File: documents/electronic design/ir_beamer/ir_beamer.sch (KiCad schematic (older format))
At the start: 42 parts, among them P1 Via, P10 Via, P2 Via, P3 Via, P4 Via, P5 Via, P7 Via, P8 Via, P9 Via, T1 2N7002K, T10 2N7002K, T11 2N7002K, T12 2N7002K, T2 2N7002K, T3 2N7002K, T4 2N7002K, T5 2N7002K, T6 2N7002K, T7 2N7002K, T8 2N7002K, T9 2N7002K, U1 74HC595D, U2 STM32F103HEADER, U3 74HC595D, U4 SE8R01_module

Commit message: update PCB projects for beamer and sensor
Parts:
- removed R1, R2, R3, R4: 4.7k, Resistors_SMD:R_0805_HandSoldering, symbol R
- added P11, P12, P13, P14, P15, P16, P17, P6: Via, footprints:Via, symbol Via
- R5: footprint (none) -> Resistors_SMD:R_0805_HandSoldering
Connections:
- net labels added: Cascade, MR_NOT, OE_NOT
- wire segments 10 -> 12
- no-connect marks 32 -> 30
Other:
- moved on the sheet: R5

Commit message: minor update in beamer pcb (added vias for pwm_gnd signal)
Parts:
- added P18, P19, P20, P21, P22, P23, P24, P25, P26, P27, P28: Via, footprints:Via, symbol Via
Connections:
- wire segments 12 -> 13

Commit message: update schema for receiver
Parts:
- removed P11, P12, P13, P15, P18, P19, P20, P21, P22, P23, P24, P25, P26, P27, P28, P6: Via, footprints:Via, symbol Via
- removed R5: 100, Resistors_SMD:R_0805_HandSoldering, symbol R
- removed T1, T10, T11, T12, T2, T3, T4, T5, T6, T7, T8, T9: 2N7002K, footprints:SOT23, symbol 2N7002K
- added R? (x4): 10K, symbol R
- added R? (x11): 50, symbol R
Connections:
- net labels removed: MR_NOT, OE_NOT, PWM_GND
- wire segments 13 -> 12
- no-connect marks 30 -> 32

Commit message: remake pcb for beamer
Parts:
- removed R? (x10): 50, symbol R
- added C2, C3: 100uf, Capacitors_SMD:C_1206_HandSoldering, symbol C
- added P11, P12, P13, P15, P18, P19, P20, P21, P6: Via, footprints:Via, symbol Via
- R1, R2, R3, R4, R5: renamed from R?; footprint (none) -> Capacitors_SMD:C_0805_HandSoldering
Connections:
- net labels added: IR_VCC
- wire segments 12 -> 36
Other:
- moved on the sheet: C1, D1, D10, D11, D2, D3, D4, D5, D6, D7, D8, D9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

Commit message: update pcb for beamer
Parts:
- removed P1, P10, P11, P12, P13, P14, P15, P16, P17, P18, P19, P2, P20, P21, P3, P4, P5, P6, P7, P8, P9: Via, footprints:Via, symbol Via
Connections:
- wire segments 36 -> 10

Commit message: fix beamer pcb
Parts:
- R1: value 50 -> 22
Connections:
- net labels added: IR_GND
- net labels removed: IR_VCC
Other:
- moved on the sheet: R1
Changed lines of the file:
@@
 F 3 "" H 1400 1150 50  0000 C CNN
 	1    1400 1150
-	-1   0    0    1
+	1    0    0    -1
 $EndComp
 Text Notes 8800 1650 0    60   ~ 0
@@
 F 3 "" H 1400 1750 50  0000 C CNN
 	1    1400 1750
-	-1   0    0    1
+	1    0    0    -1
 $EndComp
 Text GLabel 1600 1750 2    60   Input ~ 0
@@
 F 3 "" H 1400 2350 50  0000 C CNN
 	1    1400 2350
-	-1   0    0    1
+	1    0    0    -1
 $EndComp
 Text GLabel 1600 2350 2    60   Input ~ 0
@@
 F 3 "" H 1400 2950 50  0000 C CNN
 	1    1400 2950
-	-1   0    0    1
+	1    0    0    -1
 $EndComp
 Text GLabel 1600 2950 2    60   Input ~ 0
@@
 F 3 "" H 1400 3550 50  0000 C CNN
 	1    1400 3550
-	-1   0    0    1
+	1    0    0    -1
 $EndComp
 Text GLabel 1600 3550 2    60   Input ~ 0
@@
 F 3 "" H 1400 4150 50  0000 C CNN
 	1    1400 4150
-	-1   0    0    1
+	1    0    0    -1
 $EndComp
 Text GLabel 1600 4150 2    60   Input ~ 0
@@
 F 3 "" H 1400 4750 50  0000 C CNN
 	1    1400 4750
-	-1   0    0    1
+	1    0    0    -1
 $EndComp
 Text GLabel 1600 4750 2    60   Input ~ 0
@@
 F 3 "" H 1400 5350 50  0000 C CNN
 	1    1400 5350
-	-1   0    0    1
+	1    0    0    -1
 $EndComp
 Text GLabel 1600 5350 2    60   Input ~ 0
@@
 F 3 "" H 1400 5950 50  0000 C CNN
 	1    1400 5950
-	-1   0    0    1
+	1    0    0    -1
 $EndComp
 Text GLabel 1600 5950 2    60   Input ~ 0
@@
 F 3 "" H 1400 6550 50  0000 C CNN
 	1    1400 6550
-	-1   0    0    1
+	1    0    0    -1
 $EndComp
 Text GLabel 1600 6550 2    60   Input ~ 0
@@
 F 3 "" H 1400 7150 50  0000 C CNN
 	1    1400 7150
-	-1   0    0    1
+	1    0    0    -1
 $EndComp
 Text GLabel 4700 2700 2    60   Input ~ 0
@@
 	1    0    0    -1
 $EndComp
-$Comp
-L +5V #PWR012
-U 1 1 5791C22D
-P 1000 700
-F 0 "#PWR012" H 1000 550 50  0001 C CNN
-F 1 "+5V" H 1000 840 50  0000 C CNN
-F 2 "" H 1000 700 50  0000 C CNN
-F 3 "" H 1000 700 50  0000 C CNN
-	1    1000 700
-	0    -1   -1   0
-$EndComp
 Text GLabel 4700 1350 2    60   Input ~ 0
 Cascade
@@
 L R R1
 U 1 1 57A138ED
-P 1150 700
-F 0 "R1" V 1230 700 50  0000 C CNN
-F 1 "50" V 1150 700 50  0000 C CNN
-F 2 "Capacitors_SMD:C_0805_HandSoldering" V 1080 700 50  0001 C CNN
-F 3 "" H 1150 700 50  0000 C CNN
-	1    1150 700
-	0    1    1    0
-$EndComp
-Text GLabel 1300 700  2    60   Input ~ 0
-IR_VCC
-Text GLabel 1200 1150 0    60   Input ~ 0
-IR_VCC
-Text GLabel 1200 1750 0    60   Input ~ 0
-IR_VCC
-Text GLabel 1200 2350 0    60   Input ~ 0
-IR_VCC
-Text GLabel 1200 2950 0    60   Input ~ 0
-IR_VCC
-Text GLabel 1200 3550 0    60   Input ~ 0
-IR_VCC
-Text GLabel 1200 4150 0    60   Input ~ 0
-IR_VCC
-Text GLabel 1200 4750 0    60   Input ~ 0
-IR_VCC
-Text GLabel 1200 5350 0    60   Input ~ 0
-IR_VCC
-Text GLabel 1200 5950 0    60   Input ~ 0
-IR_VCC
-Text GLabel 1200 6550 0    60   Input ~ 0
-IR_VCC
-Text GLabel 1200 7150 0    60   Input ~ 0
-IR_VCC
+P 1350 700
+F 0 "R1" V 1430 700 50  0000 C CNN
+F 1 "22" V 1350 700 50  0000 C CNN
+F 2 "Capacitors_SMD:C_0805_HandSoldering" V 1280 700 50  0001 C CNN
+F 3 "" H 1350 700 50  0000 C CNN
+	1    1350 700
+	0    1    1    0
+$EndComp
+Text GLabel 1500 700  2    60   Input ~ 0
+IR_GND
 Text GLabel 3800 3000 0    60   Input ~ 0
 IR_LED_DATA
@@
 	5200 2900 4700 2900
 NoConn ~ 3800 750
+$Comp
+L GND #PWR?
+U 1 1 57AB0120
+P 1200 700
+F 0 "#PWR?" H 1200 450 50  0001 C CNN
+F 1 "GND" H 1200 550 50  0000 C CNN
+F 2 "" H 1200 700 50  0000 C CNN
+F 3 "" H 1200 700 50  0000 C CNN
+	1    1200 700
+	0    1    1    0
+$EndComp
+Text GLabel 1200 1150 0    60   Input ~ 0
+IR_GND
+Text GLabel 1200 1750 0    60   Input ~ 0
+IR_GND
+Text GLabel 1200 2350 0    60   Input ~ 0
+IR_GND
+Text GLabel 1200 2950 0    60   Input ~ 0
+IR_GND
+Text GLabel 1200 3550 0    60   Input ~ 0
+IR_GND
+Text GLabel 1200 4150 0    60   Input ~ 0
+IR_GND
+Text GLabel 1200 4750 0    60   Input ~ 0
+IR_GND
+Text GLabel 1200 5350 0    60   Input ~ 0
+IR_GND
+Text GLabel 1200 5950 0    60   Input ~ 0
+IR_GND
+Text GLabel 1200 6550 0    60   Input ~ 0
+IR_GND
+Text GLabel 1200 7150 0    60   Input ~ 0
+IR_GND
 $EndSCHEMATC

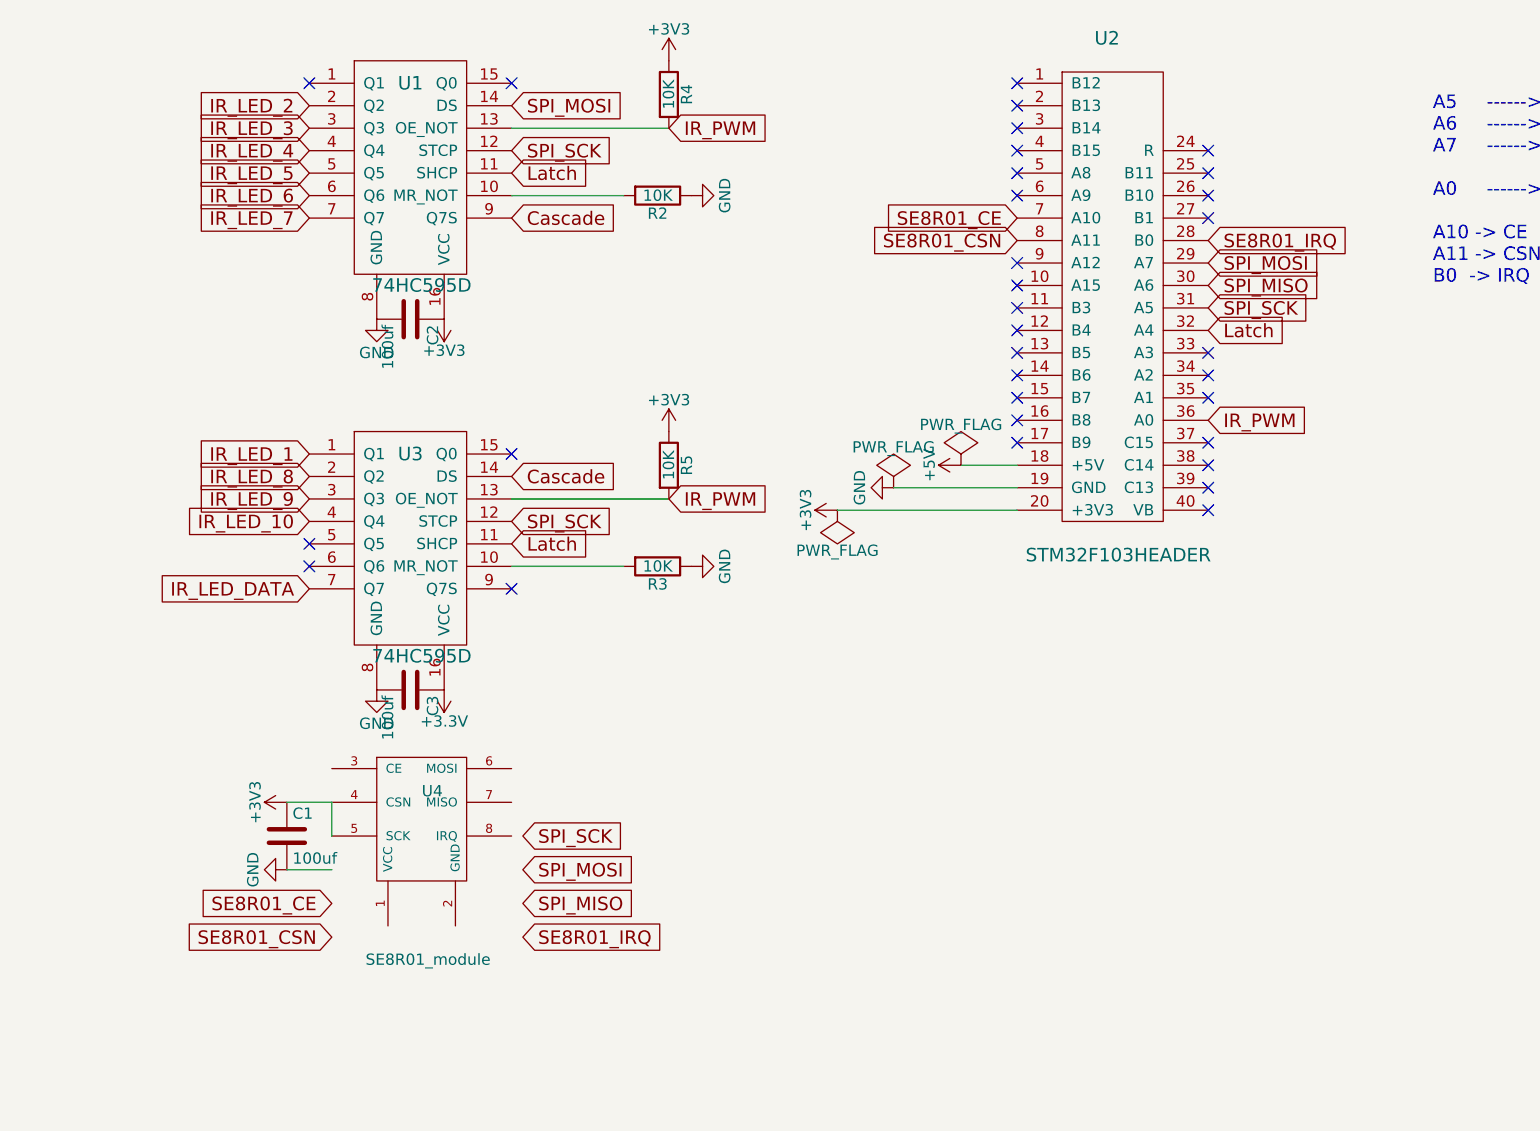
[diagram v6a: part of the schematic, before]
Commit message: make pcb for 11 leds
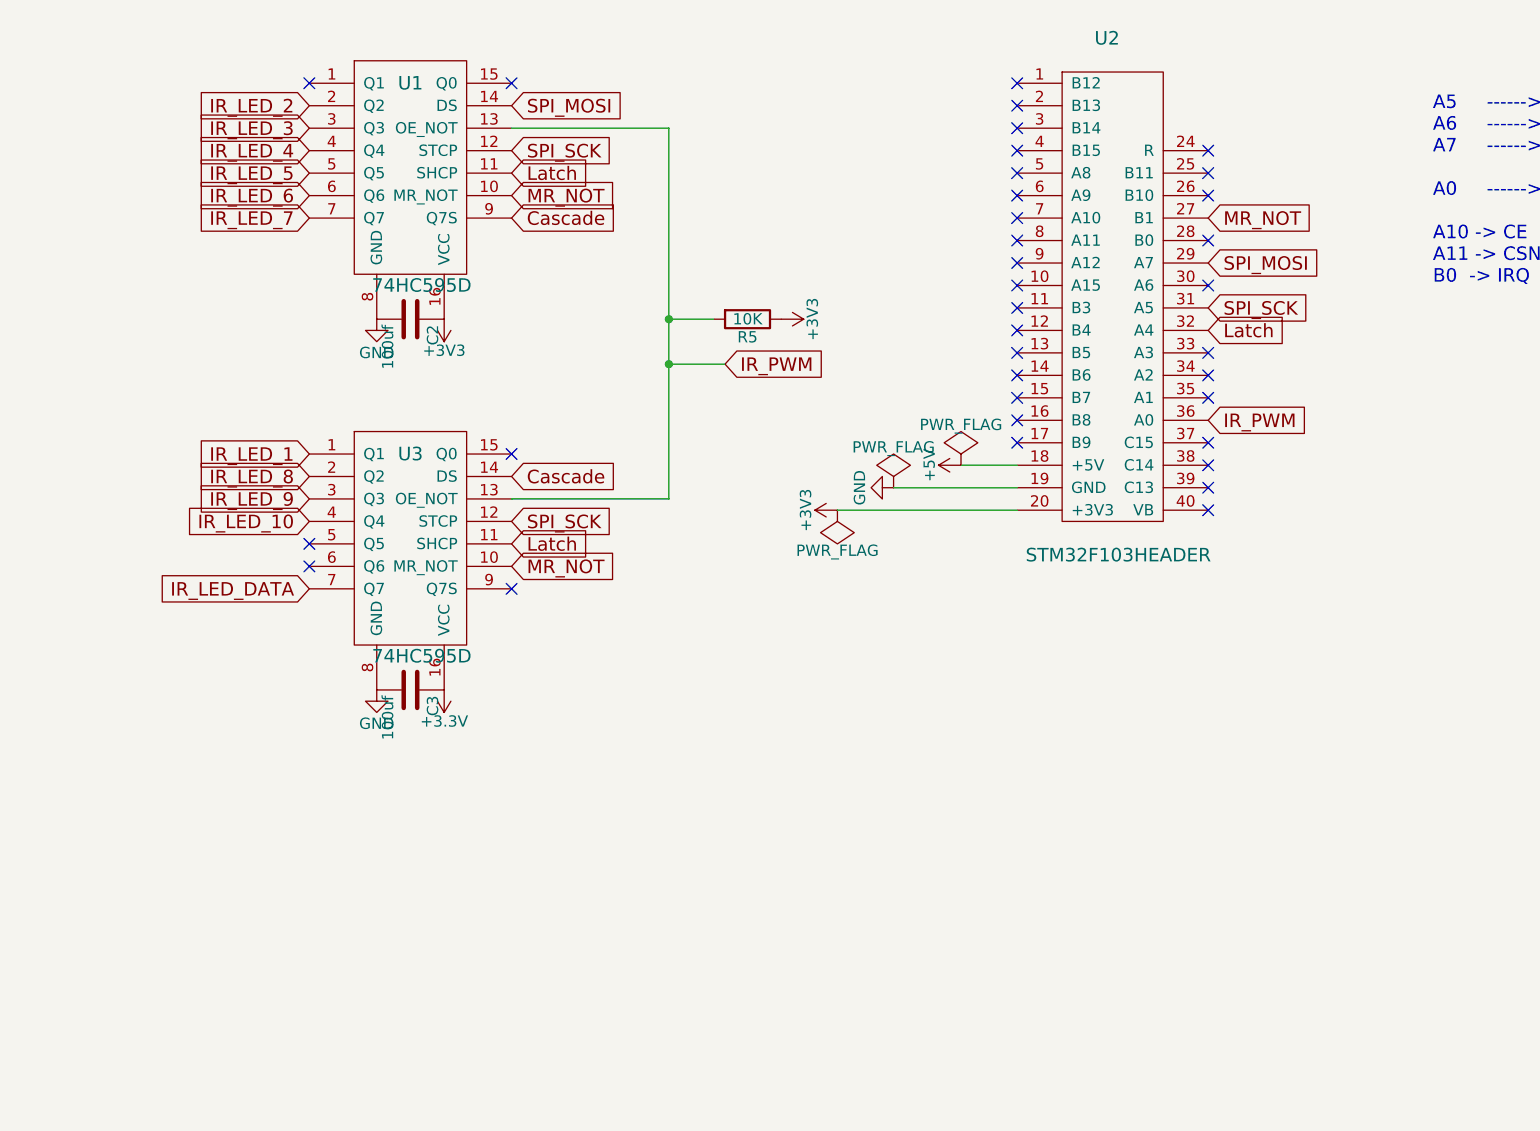
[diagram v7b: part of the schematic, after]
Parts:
- removed C1: 100uf, Capacitors_SMD:C_1206_HandSoldering, symbol C
- removed R2, R3, R4: 10K, Capacitors_SMD:C_0805_HandSoldering, symbol R
- removed U4: SE8R01_module, footprints:SE8R01_SMD, symbol SE8R01_module
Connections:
- net labels added: MR_NOT
- net labels removed: SE8R01_CE, SE8R01_CSN, SE8R01_IRQ, SPI_MISO
- wire segments 10 -> 8
- no-connect marks 32 -> 35
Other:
- moved on the sheet: R5
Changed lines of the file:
@@
 SPI_MOSI
 NoConn ~ 6950 1250
-NoConn ~ 7800 1350
 Text GLabel 3800 2400 0    60   Input ~ 0
 IR_LED_1
@@
 	-1   0    0    1
 $EndComp
-$Comp
-L SE8R01_module U4
-U 1 1 578FCE1F
-P 4500 4350
-F 0 "U4" H 4300 4800 50  0000 L CNN
-F 1 "SE8R01_module" H 4050 4050 50  0000 L CNN
-F 2 "footprints:SE8R01_SMD" H 4200 4700 50  0001 L CNN
-F 3 "" H 4550 4350 60  0000 C CNN
-	1    4500 4350
-	1    0    0    -1
-$EndComp
-$Comp
-L +3V3 #PWR08
-U 1 1 578FD7B5
-P 3700 3950
-F 0 "#PWR08" H 3700 3800 50  0001 C CNN
-F 1 "+3V3" H 3700 4090 50  0000 C CNN
-F 2 "" H 3700 3950 50  0000 C CNN
-F 3 "" H 3700 3950 50  0000 C CNN
-	1    3700 3950
-	0    -1   -1   0
-$EndComp
-$Comp
-L GND #PWR09
-U 1 1 578FDB5C
-P 3700 4250
-F 0 "#PWR09" H 3700 4000 50  0001 C CNN
-F 1 "GND" H 3700 4100 50  0000 C CNN
-F 2 "" H 3700 4250 50  0000 C CNN
-F 3 "" H 3700 4250 50  0000 C CNN
-	1    3700 4250
-	0    1    1    0
-$EndComp
-$Comp
-L C C1
-U 1 1 578FDDE6
-P 3700 4100
-F 0 "C1" H 3725 4200 50  0000 L CNN
-F 1 "100uf" H 3725 4000 50  0000 L CNN
-F 2 "Capacitors_SMD:C_1206_HandSoldering" H 3738 3950 50  0001 C CNN
-F 3 "" H 3700 4100 50  0000 C CNN
-	1    3700 4100
-	1    0    0    -1
-$EndComp
-Text GLabel 3900 4400 0    60   Input ~ 0
-SE8R01_CE
-Text GLabel 3900 4550 0    60   Input ~ 0
-SE8R01_CSN
-Text GLabel 4750 4100 2    60   Input ~ 0
-SPI_SCK
-Text GLabel 4750 4400 2    60   Input ~ 0
-SPI_MISO
-Text GLabel 7800 1650 2    60   Input ~ 0
-SPI_MISO
-Text GLabel 4750 4550 2    60   Input ~ 0
-SE8R01_IRQ
-Text GLabel 7800 1450 2    60   Input ~ 0
-SE8R01_IRQ
-Text GLabel 6950 1350 0    60   Input ~ 0
-SE8R01_CE
-Text GLabel 6950 1450 0    60   Input ~ 0
-SE8R01_CSN
 NoConn ~ 7800 1950
 Text GLabel 4700 2800 2    60   Input ~ 0
 Latch
-Text GLabel 4750 4250 2    60   Input ~ 0
-SPI_MOSI
 Text GLabel 4700 1150 2    60   Input ~ 0
 Latch
 $Comp
-L +5V #PWR010
+L +5V #PWR08
 U 1 1 57910C6F
 P 6700 2450
-F 0 "#PWR010" H 6700 2300 50  0001 C CNN
+F 0 "#PWR08" H 6700 2300 50  0001 C CNN
 F 1 "+5V" H 6700 2590 50  0000 C CNN
 F 2 "" H 6700 2450 50  0000 C CNN
@@
 $EndComp
 $Comp
-L PWR_FLAG #FLG011
+L PWR_FLAG #FLG09
 U 1 1 57910CFC
 P 6700 2450
-F 0 "#FLG011" H 6700 2545 50  0001 C CNN
+F 0 "#FLG09" H 6700 2545 50  0001 C CNN
 F 1 "PWR_FLAG" H 6700 2630 50  0000 C CNN
 F 2 "" H 6700 2450 50  0000 C CNN
@@
 NoConn ~ 6950 1750
 NoConn ~ 6950 1850
-Text GLabel 5400 950  2    60   Input ~ 0
+Text GLabel 5650 2000 2    60   Input ~ 0
 IR_PWM
 $Comp
-L +3V3 #PWR013
-U 1 1 57A11085
-P 5400 650
-F 0 "#PWR013" H 5400 500 50  0001 C CNN
-F 1 "+3V3" H 5400 790 50  0000 C CNN
-F 2 "" H 5400 650 50  0000 C CNN
-F 3 "" H 5400 650 50  0000 C CNN
-	1    5400 650
-	1    0    0    -1
-$EndComp
-$Comp
-L R R4
-U 1 1 57A11104
-P 5400 800
-F 0 "R4" V 5480 800 50  0000 C CNN
-F 1 "10K" V 5400 800 50  0000 C CNN
-F 2 "Capacitors_SMD:C_0805_HandSoldering" V 5330 800 50  0001 C CNN
-F 3 "" H 5400 800 50  0000 C CNN
-	1    5400 800
-	1    0    0    -1
-$EndComp
-Text GLabel 5400 2600 2    60   Input ~ 0
-IR_PWM
-$Comp
-L +3V3 #PWR014
+L +3V3 #PWR010
 U 1 1 57A116F2
-P 5400 2300
-F 0 "#PWR014" H 5400 2150 50  0001 C CNN
-F 1 "+3V3" H 5400 2440 50  0000 C CNN
-F 2 "" H 5400 2300 50  0000 C CNN
-F 3 "" H 5400 2300 50  0000 C CNN
-	1    5400 2300
-	1    0    0    -1
+P 5900 1800
+F 0 "#PWR010" H 5900 1650 50  0001 C CNN
+F 1 "+3V3" H 5900 1940 50  0000 C CNN
+F 2 "" H 5900 1800 50  0000 C CNN
+F 3 "" H 5900 1800 50  0000 C CNN
+	1    5900 1800
+	0    1    1    0
 $EndComp
 $Comp
 L R R5
 U 1 1 57A116F8
-P 5400 2450
-F 0 "R5" V 5480 2450 50  0000 C CNN
-F 1 "10K" V 5400 2450 50  0000 C CNN
-F 2 "Capacitors_SMD:C_0805_HandSoldering" V 5330 2450 50  0001 C CNN
-F 3 "" H 5400 2450 50  0000 C CNN
-	1    5400 2450
-	1    0    0    -1
-$EndComp
-$Comp
-L R R3
-U 1 1 57A11C3B
-P 5350 2900
-F 0 "R3" V 5430 2900 50  0000 C CNN
-F 1 "10K" V 5350 2900 50  0000 C CNN
-F 2 "Capacitors_SMD:C_0805_HandSoldering" V 5280 2900 50  0001 C CNN
-F 3 "" H 5350 2900 50  0000 C CNN
-	1    5350 2900
-	0    1    1    0
-$EndComp
-$Comp
-L R R2
-U 1 1 57A11D31
-P 5350 1250
-F 0 "R2" V 5430 1250 50  0000 C CNN
-F 1 "10K" V 5350 1250 50  0000 C CNN
-F 2 "Capacitors_SMD:C_0805_HandSoldering" V 5280 1250 50  0001 C CNN
-F 3 "" H 5350 1250 50  0000 C CNN
-	1    5350 1250
-	0    1    1    0
-$EndComp
-$Comp
-L GND #PWR015
-U 1 1 57A11E8E
-P 5500 1250
-F 0 "#PWR015" H 5500 1000 50  0001 C CNN
-F 1 "GND" H 5500 1100 50  0000 C CNN
-F 2 "" H 5500 1250 50  0000 C CNN
-F 3 "" H 5500 1250 50  0000 C CNN
-	1    5500 1250
-	0    -1   -1   0
-$EndComp
-$Comp
-L GND #PWR016
-U 1 1 57A11F50
-P 5500 2900
-F 0 "#PWR016" H 5500 2650 50  0001 C CNN
-F 1 "GND" H 5500 2750 50  0000 C CNN
-F 2 "" H 5500 2900 50  0000 C CNN
-F 3 "" H 5500 2900 50  0000 C CNN
-	1    5500 2900
-	0    -1   -1   0
+P 5750 1800
+F 0 "R5" V 5830 1800 50  0000 C CNN
+F 1 "10K" V 5750 1800 50  0000 C CNN
+F 2 "Capacitors_SMD:C_0805_HandSoldering" V 5680 1800 50  0001 C CNN
+F 3 "" H 5750 1800 50  0000 C CNN
+	1    5750 1800
+	0    1    1    0
 $EndComp
 Text GLabel 1600 1150 2    60   Input ~ 0
@@
 NoConn ~ 4700 750
 $Comp
-L GND #PWR017
+L GND #PWR011
 U 1 1 5787C121
 P 4100 1800
-F 0 "#PWR017" H 4100 1550 50  0001 C CNN
+F 0 "#PWR011" H 4100 1550 50  0001 C CNN
 F 1 "GND" H 4100 1650 50  0000 C CNN
 F 2 "" H 4100 1800 50  0000 C CNN
@@
 $EndComp
 Wire Wire Line
-	3900 4250 3700 4250
-Wire Wire Line
-	5200 1250 4700 1250
-Wire Wire Line
-	5400 2600 4700 2600
-Wire Wire Line
 	5400 950  4700 950
 Wire Wire Line
-	3700 3950 3900 3950
-Wire Wire Line
 	6950 2650 6150 2650
 Wire Wire Line
-	3900 3950 3900 4100
-Wire Wire Line
 	6400 2550 6950 2550
 Wire Wire Line
 	6950 2450 6700 2450
-Wire Wire Line
-	5200 2900 4700 2900
 NoConn ~ 3800 750
 $Comp
-L GND #PWR?
+L GND #PWR012
 U 1 1 57AB0120
 P 1200 700
-F 0 "#PWR?" H 1200 450 50  0001 C CNN
+F 0 "#PWR012" H 1200 450 50  0001 C CNN
 F 1 "GND" H 1200 550 50  0000 C CNN
 F 2 "" H 1200 700 50  0000 C CNN
@@
 Text GLabel 1200 7150 0    60   Input ~ 0
 IR_GND
+Text GLabel 4700 2900 2    60   Input ~ 0
+MR_NOT
+Text GLabel 4700 1250 2    60   Input ~ 0
+MR_NOT
+Text GLabel 7800 1350 2    60   Input ~ 0
+MR_NOT
+Wire Wire Line
+	4700 2600 5400 2600
+Wire Wire Line
+	5400 2600 5400 950
+NoConn ~ 7800 1650
+NoConn ~ 6950 1450
+NoConn ~ 6950 1350
+NoConn ~ 7800 1450
+Wire Wire Line
+	5600 1800 5400 1800
+Connection ~ 5400 1800
+Wire Wire Line
+	5650 2000 5400 2000
+Connection ~ 5400 2000
 $EndSCHEMATC
